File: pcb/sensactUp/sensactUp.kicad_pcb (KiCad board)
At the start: 2 copper layers, 71 x 71 mm, 65 parts, among them P1 CONN_01X06, P10 3V3, P11 CONN_02X05, P16 5V, P2 PWR, P3 CAN, P4 3V3, P5 ROT2EXT, P6 GND, P7 CONN_01X06, P8 GND, P9 5V, SW1 ROTARY_ENCODER_SWITCH_CASE, SW2 RESET, U1 LMR14006, U2 LMR14006, U3 STM32F072C8Tx, U9 SN65HVD230, Y1 Crystal_GND24

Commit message: Minor improvement in PCB
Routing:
- net IO1: track 20.8 -> 22.5 mm
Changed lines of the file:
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@@
     (thickness 1.6)
     (drawings 112)
-    (tracks 636)
+    (tracks 643)
     (zones 0)
     (modules 65)
@@
   (page A4)
   (layers
-    (0 F.Cu signal)
+    (0 F.Cu signal hide)
     (31 B.Cu signal)
-    (32 B.Adhes user)
+    (32 B.Adhes user hide)
     (33 F.Adhes user)
-    (34 B.Paste user)
+    (34 B.Paste user hide)
     (35 F.Paste user)
-    (36 B.SilkS user)
-    (37 F.SilkS user)
-    (38 B.Mask user)
-    (39 F.Mask user)
+    (36 B.SilkS user hide)
+    (37 F.SilkS user hide)
+    (38 B.Mask user hide)
+    (39 F.Mask user hide)
     (40 Dwgs.User user)
-    (41 Cmts.User user)
-    (42 Eco1.User user)
-    (43 Eco2.User user)
-    (44 Edge.Cuts user)
-    (45 Margin user)
+    (41 Cmts.User user hide)
+    (42 Eco1.User user hide)
+    (43 Eco2.User user hide)
+    (44 Edge.Cuts user hide)
+    (45 Margin user hide)
     (46 B.CrtYd user hide)
     (47 F.CrtYd user hide)
-    (48 B.Fab user)
-    (49 F.Fab user)
+    (48 B.Fab user hide)
+    (49 F.Fab user hide)
   )
   (setup
@@
   (segment (start 147.762636 81.534) (end 149.352 81.534) (width 0.2032) (layer B.Cu) (net 29))
   (segment (start 141.381002 87.915634) (end 147.762636 81.534) (width 0.2032) (layer B.Cu) (net 29))
+  (segment (start 135.973 92.836) (end 135.973 90.910636) (width 0.2032) (layer B.Cu) (net 30))
+  (segment (start 136.586636 90.297) (end 137.541 90.297) (width 0.2032) (layer B.Cu) (net 30))
+  (segment (start 135.973 90.910636) (end 136.586636 90.297) (width 0.2032) (layer B.Cu) (net 30))
+  (segment (start 137.922 90.297) (end 147.447 80.772) (width 0.2032) (layer B.Cu) (net 30))
+  (segment (start 137.541 90.297) (end 137.922 90.297) (width 0.2032) (layer B.Cu) (net 30))
+  (segment (start 147.447 80.772) (end 147.447 80.391) (width 0.2032) (layer B.Cu) (net 30))
   (segment (start 135.973 92.836) (end 135.973 92.246) (width 0.2032) (layer B.Cu) (net 30))
-  (segment (start 135.973 92.246) (end 147.447 80.772) (width 0.2032) (layer B.Cu) (net 30))
-  (segment (start 147.447 80.772) (end 147.447 78.613) (width 0.2032) (layer B.Cu) (net 30))
+  (segment (start 147.447 80.772) (end 147.447 80.391) (width 0.2032) (layer B.Cu) (net 30))
+  (segment (start 147.447 80.391) (end 147.447 78.613) (width 0.2032) (layer B.Cu) (net 30))
   (segment (start 147.447 78.613) (end 148.73 77.33) (width 0.2032) (layer B.Cu) (net 30))
   (segment (start 148.73 80.027818) (end 142.699909 86.057909) (width 0.2032) (layer B.Cu) (net 31))
@@
   (segment (start 132.973 92.836) (end 132.973 89.865) (width 0.2032) (layer B.Cu) (net 46))
   (segment (start 132.973 89.865) (end 133.858 88.98) (width 0.2032) (layer B.Cu) (net 46))
+  (segment (start 135.473 92.836) (end 135.473 90.871818) (width 0.2032) (layer B.Cu) (net 47))
+  (segment (start 136.682818 89.662) (end 137.287 89.662) (width 0.2032) (layer B.Cu) (net 47))
+  (segment (start 135.473 90.871818) (end 136.682818 89.662) (width 0.2032) (layer B.Cu) (net 47))
   (segment (start 149.987 95.123) (end 149.987 94.98574) (width 0.2032) (layer B.Cu) (net 47))
   (segment (start 149.987 94.98574) (end 147.50064 92.49938) (width 0.2032) (layer B.Cu) (net 47))
   (segment (start 144.018 89.662) (end 146.7955 89.662) (width 0.2032) (layer B.Cu) (net 47))
-  (segment (start 135.473 92.836) (end 135.473 91.476) (width 0.2032) (layer B.Cu) (net 47))
-  (via (at 144.018 89.662) (size 0.6096) (drill 0.3048) (layers F.Cu B.Cu) (net 47))
-  (segment (start 137.287 89.662) (end 144.018 89.662) (width 0.2032) (layer F.Cu) (net 47))
-  (via (at 137.287 89.662) (size 0.6096) (drill 0.3048) (layers F.Cu B.Cu) (net 47))
-  (segment (start 135.473 91.476) (end 137.287 89.662) (width 0.2032) (layer B.Cu) (net 47))
   (segment (start 146.7955 89.662) (end 147.5105 90.377) (width 0.2032) (layer B.Cu) (net 47))
+  (via (at 137.287 89.662) (size 0.6096) (drill 0.3048) (layers F.Cu B.Cu) (net 47))
+  (segment (start 137.287 89.662) (end 144.018 89.662) (width 0.2032) (layer F.Cu) (net 47))
+  (via (at 144.018 89.662) (size 0.6096) (drill 0.3048) (layers F.Cu B.Cu) (net 47))
   (segment (start 147.5105 90.377) (end 147.5105 92.48952) (width 0.2032) (layer B.Cu) (net 47))
   (segment (start 147.5105 92.48952) (end 147.50064 92.49938) (width 0.2032) (layer B.Cu) (net 47))

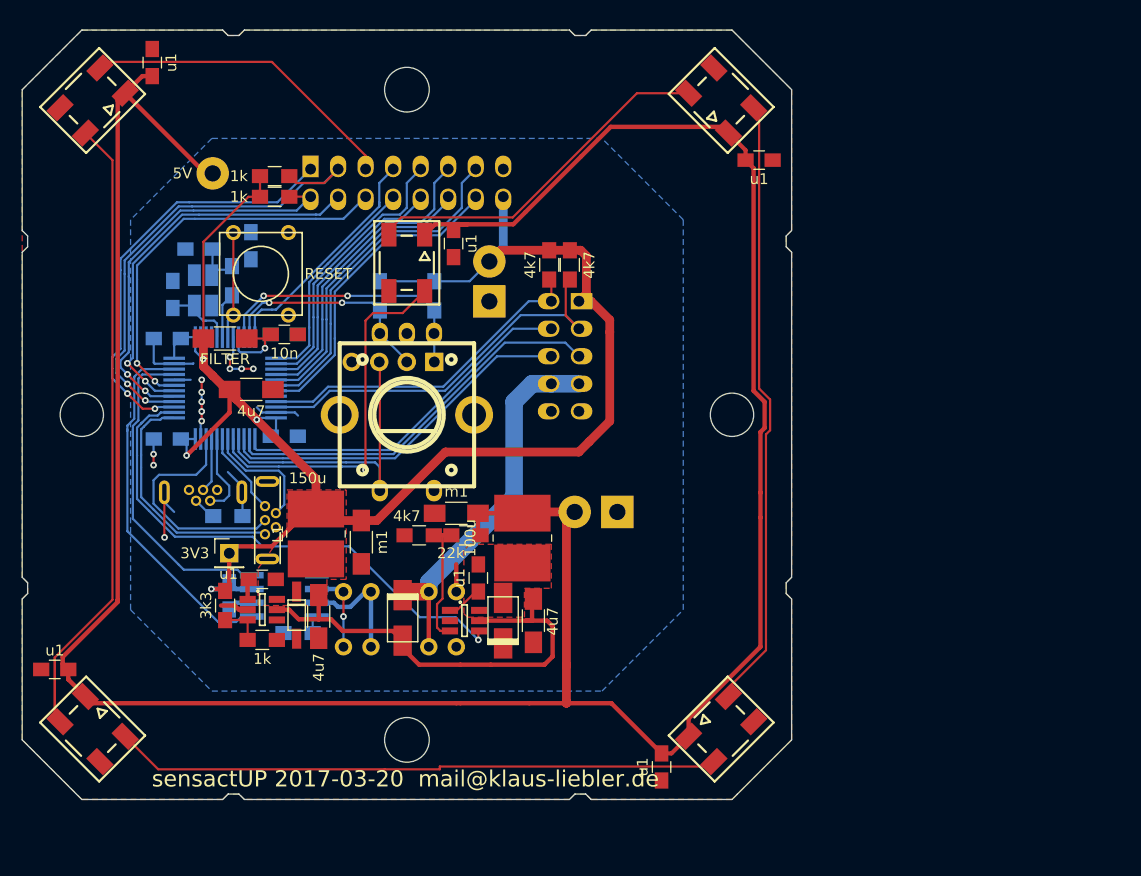
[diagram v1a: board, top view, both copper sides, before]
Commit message: SensactUP gets LIN-Port and alternative 5V Power Supply
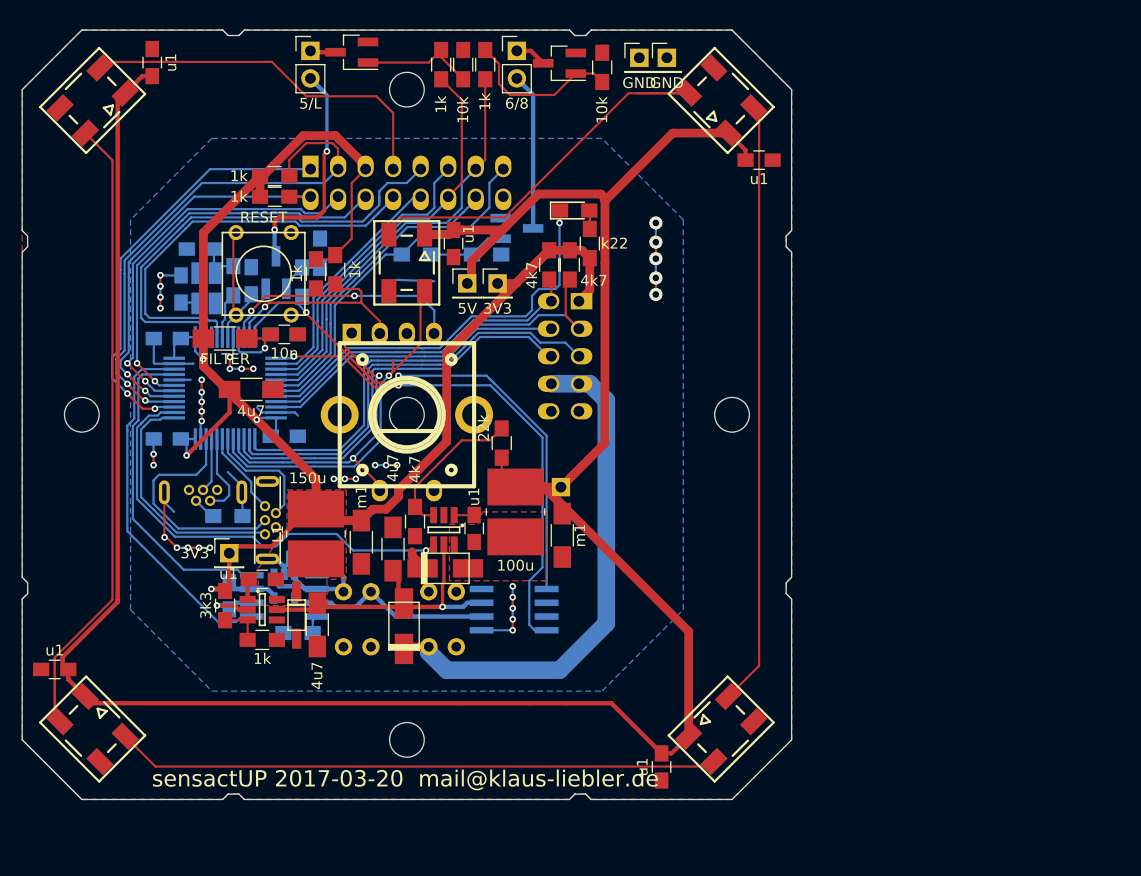
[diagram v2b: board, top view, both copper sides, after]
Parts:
- added C21: u1, Capacitors_SMD:C_0805_HandSoldering, B.Cu at (140.8, 113.2)
- added D9: LED, sensact:LED_0805_handsolder, F.Cu at (165.5, 81.2)
- added MK1: Mounting_Hole, Mounting_Holes:MountingHole_3.2mm_M3, F.Cu at (150.0, 100.0)
- added MK2: Mounting_Hole, Mounting_Holes:MountingHole_3.2mm_M3, F.Cu at (180.0, 100.0)
- added MK3: Mounting_Hole, Mounting_Holes:MountingHole_3.2mm_M3, F.Cu at (120.0, 100.0)
- added MK4: Mounting_Hole, Mounting_Holes:MountingHole_3.2mm_M3, F.Cu at (150.0, 130.0)
- added MK5: Mounting_Hole, Mounting_Holes:MountingHole_3.2mm_M3, F.Cu at (150.0, 70.0)
- added P12: 6/8, Pin_Headers:Pin_Header_Straight_1x02_Pitch2.54mm, F.Cu at (160.1, 66.4)
- added P13: 5/L, Pin_Headers:Pin_Header_Straight_1x02_Pitch2.54mm, F.Cu at (141.1, 66.4)
- added Q1: Q_NMOS_GSD, TO_SOT_Packages_SMD:SOT-23_Handsoldering, B.Cu at (160.1, 82.8)
- added Q2: Q_NMOS_GSD, TO_SOT_Packages_SMD:SOT-23_Handsoldering, F.Cu at (164.1, 67.6)
- added Q3: Q_NMOS_GSD, TO_SOT_Packages_SMD:SOT-23_Handsoldering, F.Cu at (144.9, 66.5)
- added Q4: Q_NMOS_GSD, TO_SOT_Packages_SMD:SOT-23_Handsoldering, B.Cu at (137.9, 86.9)
- added R11: 1k, Resistors_SMD:R_0805_HandSoldering, B.Cu at (150.9, 85.2)
- added R16: 10k, Resistors_SMD:R_0805_HandSoldering, B.Cu at (157.4, 85.2)
- added R17: 1k, Resistors_SMD:R_0805_HandSoldering, F.Cu at (157.2, 67.7)
- added R18: 10k, Resistors_SMD:R_0805_HandSoldering, F.Cu at (168.0, 67.9)
- added R19: 1k, Resistors_SMD:R_0805_HandSoldering, F.Cu at (153.2, 67.7)
- added R20: 10k, Resistors_SMD:R_0805_HandSoldering, F.Cu at (155.2, 67.7)
- added R21: 1k, Resistors_SMD:R_0805_HandSoldering, B.Cu at (140.3, 87.8)
- added R22: 10k, Resistors_SMD:R_0805_HandSoldering, B.Cu at (142.0, 85.1)
- added R9: k22, Resistors_SMD:R_0805_HandSoldering, F.Cu at (166.9, 84.2)
- added U4: TLV70033DDC, TO_SOT_Packages_SMD:SOT-23-5, B.Cu at (138.7, 115.8)
- added U5: TJA1021T, sensact:SOIC-8_3.9x4.9mm_Pitch1.27mm_handsolder, B.Cu at (159.9, 118.0)
- C22: value u1 -> u1_1u
- P16, P9: footprint Measurement_Points:Measurement_Point_Round-TH_Big -> Pin_Headers:Pin_Header_Straight_1x01_Pitch2.54mm
- P2, P3: footprint sensact:KF141R-2p -> sensact:KF141R-2p_1234
- P4: footprint Measurement_Points:Measurement_Point_Round-TH_Big -> Pin_Headers:Pin_Header_Straight_1x01_Pitch2.54mm; moved to F.Cu
- P5: footprint Pin_Headers:Pin_Header_Straight_1x04_Pitch2.54mm -> Pin_Headers:Pin_Header_Straight_1x01_Pitch2.54mm
- P6, P8: footprint Measurement_Points:Measurement_Point_Square-TH_Big -> Pin_Headers:Pin_Header_Straight_1x01_Pitch2.54mm; moved to F.Cu
- R13, R15: moved to F.Cu
- moved P6 42.2 mm to (174.0, 67.1)
- moved P8 26.4 mm to (171.4, 67.1)
- moved P9 25.6 mm to (155.6, 87.9)
- moved C2 14.5 mm to (148.7, 112.4), turned to 90 degrees
- moved R15 11.1 mm to (141.6, 87.0)
- moved C6 9.99 mm to (164.3, 111.1), turned to 270 degrees
- moved R2 9.13 mm to (158.8, 102.6), turned to 90 degrees
- moved U1 8.60 mm to (153.4, 110.6), turned to 270 degrees
- moved P5 8.07 mm to (144.9, 92.5), turned to 270 degrees
- moved D1 7.19 mm to (153.5, 114.2), turned to 180 degrees
- moved R13 4.78 mm to (143.4, 86.6)
- moved C4 4.59 mm to (156.2, 110.5), turned to 90 degrees
- moved C9 3.23 mm to (135.6, 87.6), turned to 270 degrees
- moved P16 2.62 mm to (164.2, 106.7)
- moved L2 2.50 mm to (160.0, 109.0)
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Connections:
- O1 pad 10: IO4 -> IO3
- O1 pad 11: IO5 -> IO4
- O1 pad 12: IO6 -> IO5
- O1 pad 13: IO7 -> IO6
- O1 pad 14: IO8 -> IO7
- O1 pad 15: GND -> IO8
- O1 pad 16: +3V3 -> GND
- O1 pad 5: /WS2812OUT -> +3V3
- O1 pad 7: IO1 -> /WS2812OUT
- O1 pad 8: IO2 -> IO1
- O1 pad 9: IO3 -> IO2
- P2 pad 2: GND -> (no net)
- P3 pad 1: /CANL -> (no net)
- P3 pad 2: /CANH -> /CANL_5V
- P5 pad 1: ROTA -> ROTD
- U3 pad 12: IO1 -> LINTX
- U3 pad 13: IO2 -> LINRX
- U3 pad 2: (no net) -> IO2
- U3 pad 20: (no net) -> /cpu/LED
- U3 pad 3: (no net) -> IO1
- U9 pad 6: /CANL -> /CANL_5V
- U9 pad 7: /CANH -> /CANH_LIN
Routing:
- net LINTX: track 0.00 -> 50.7 mm, vias 0 -> 2
- net LINRX: track 0.00 -> 48.6 mm, vias 0 -> 2
- net /cpu/LED: track 0.00 -> 38.3 mm, vias 0 -> 1
- net GND: track 43.4 -> 76.9 mm, vias 12 -> 37
- net /O24_4: track 0.00 -> 23.0 mm, vias 0 -> 2
- net IO2: track 20.5 -> 42.7 mm
- net +5V: track 256.3 -> 237.2 mm
- net /CANH_LIN: track 0.00 -> 16.9 mm
- net IO1: track 22.5 -> 37.5 mm
- net Net-(Q2-Pad1): track 0.00 -> 14.7 mm
- net /O24_1: track 0.00 -> 14.5 mm
- net +24V: track 43.0 -> 29.0 mm, vias 0 -> 1
- net /CANL_5V: track 0.00 -> 13.1 mm
- net /24VX: track 35.1 -> 48.0 mm
- net IO6: track 26.6 -> 39.2 mm
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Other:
- outline, holes or cut-outs redrawn
- board text added: "CANH/LIN"
- board text added: "CANL/5V"
- board text added: "xRD xRB xRA SC1 3V3 SD1 WS1 IO1 IO2 IO3 IO4 IO5 IO6 IO7 IO8 GND"
- board text removed: "CANH"
- board text removed: "CANL"
- board text removed: "xRD xRB xRA SC1 WS2 SD1 IO1 IO2 IO3 IO4 IO5 IO6 IO7 IO8 GND 3V3"

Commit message: More Voltage pins
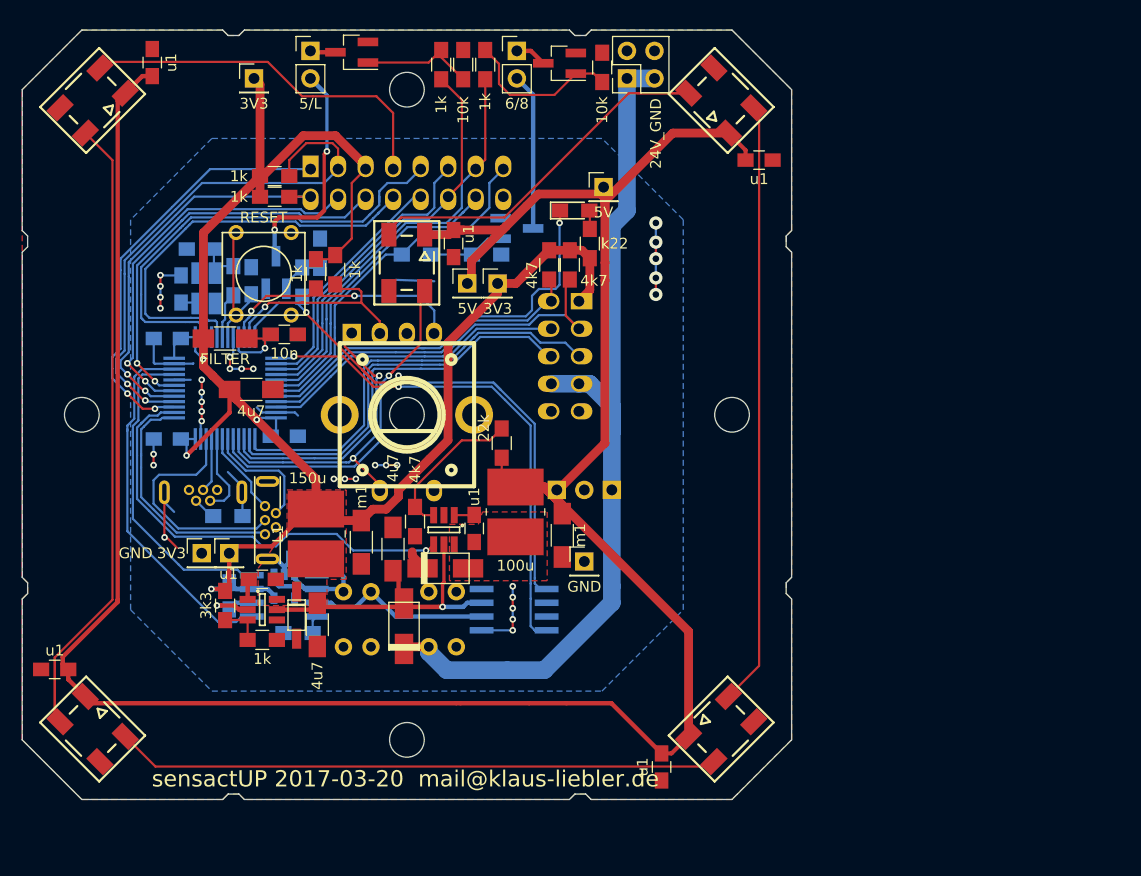
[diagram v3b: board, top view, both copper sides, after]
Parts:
- added P14: GND, Pin_Headers:Pin_Header_Straight_1x01_Pitch2.54mm, F.Cu at (166.4, 113.5)
- added P15: 5V, Pin_Headers:Pin_Header_Straight_1x01_Pitch2.54mm, F.Cu at (168.1, 79.0)
- added P17: 3V3, Pin_Headers:Pin_Header_Straight_1x01_Pitch2.54mm, F.Cu at (135.9, 69.0)
- added P18: 24V_GND, Pin_Headers:Pin_Header_Straight_1x02_Pitch2.54mm, B.Cu at (168.9, 106.9)
- P8: value GND -> 24V_GND; footprint Pin_Headers:Pin_Header_Straight_1x01_Pitch2.54mm -> Pin_Headers:Pin_Header_Straight_2x02_Pitch2.54mm
- moved P6 62.7 mm to (131.1, 112.8)
- moved P8 2.22 mm to (170.3, 69.0), turned to 90 degrees
- moved P16 0.46 mm to (163.8, 106.9)
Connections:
- P8 pad 1: GND -> /24VX
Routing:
- net /24VX: track 48.0 -> 83.4 mm
- net GND: track 76.9 -> 63.2 mm, vias 37 -> 22
- net (no net): track 3.56 -> 14.2 mm, vias 0 -> 11
- net +3V3: track 167.5 -> 172.6 mm
- net +5V: track 237.2 -> 239.5 mm
- net WS2812: track 34.0 -> 32.4 mm
- net LINTX: track 50.7 -> 51.2 mm
